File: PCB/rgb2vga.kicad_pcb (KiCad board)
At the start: 2 copper layers, 70.5 x 55.9 mm, 39 parts, among them J1 GPIO_0, J2 RGB_IN, J3 COCO3_RGB_IN, J4 C_VIDEO_IN, J5 GPIO_1, J6 VGA_OUT, SW1 SW_DIP_x12, U1 LM1881

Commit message: SW2 for Artifact
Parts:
- added SW2: SW_DP3T, 000_LOCAL:SW_DP3T_CK_JS203011JAQN, B.Cu at (143.2, 126.7)
- SW1: value SW_DIP_x12 -> SW_DIP_x10; footprint 000_LOCAL:SW_DIP_SPSTx12_Slide_6.7x32.04mm_W8.61mm_P2.54mm_LowProfile -> 000_LOCAL:SW_DIP_SPSTx10_Slide_6.7_8.61_P2.54_LowProfile
- moved R24 3.19 mm to (143.2, 117.5)
- moved SW1 1.27 mm to (130.8, 101.0)
- moved R1 0.32 mm to (155.3, 101.0)
- moved R10 0.32 mm to (155.3, 78.1)
- moved R11 0.32 mm to (155.3, 126.4)
- moved R12 0.32 mm to (155.3, 121.3)
- moved R13 0.32 mm to (155.3, 111.1)
- moved R14 0.32 mm to (155.3, 116.2)
- moved R15 0.32 mm to (155.3, 118.7)
- moved R16 0.32 mm to (155.3, 123.8)
- moved R17 0.32 mm to (155.3, 113.7)
- moved R2 0.32 mm to (155.3, 98.4)
- moved R26 0.32 mm to (155.3, 80.6)
- moved R3 0.32 mm to (155.3, 95.9)
- moved R4 0.32 mm to (155.3, 93.3)
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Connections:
- J3 pad 10: (no net) -> GND
- SW1 pad 1: (no net) -> /RGB_G
- SW1 pad 10: /SW_SCANLINE -> /_VSYNC
- SW1 pad 11: /_HSYNC -> /SW_C_VS
- SW1 pad 12: /_VSYNC -> /SW_C_HS
- SW1 pad 13: /SW_C_VS -> GND
- SW1 pad 14: /SW_C_HS -> GND
- SW1 pad 2: /RGB_G -> /SW_SHRINK
- SW1 pad 20: GND -> /RGB_CS
- SW1 pad 3: /SW_SHRINK -> /SW_MSX
- SW1 pad 4: /SW_MSX -> /SW_DEINT
- SW1 pad 5: /SW_DEINT -> /SW_APPLE_][
- SW1 pad 6: /SW_APPLE_][ -> GND
- SW1 pad 7: /SW_ARTIF_INV -> /SW_SYNC_LVL
- SW1 pad 8: /SW_ARTIFACT -> /SW_SCANLINE
- SW1 pad 9: /SW_SYNC_LVL -> /_HSYNC
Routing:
- net /SW_ARTIF_INV: track 3.71 -> 59.1 mm, vias 0 -> 1
- net /SW_ARTIFACT: track 3.71 -> 55.2 mm, vias 0 -> 1
- net /DIFF_N: track 85.2 -> 88.5 mm
- net /D0: track 30.8 -> 32.9 mm
- net /D2: track 30.8 -> 31.7 mm
- net /RGB_V: track 38.9 -> 38.0 mm
- net /RGB_CS: track 74.4 -> 73.5 mm
- net /VGA_B: track 44.0 -> 43.4 mm
- net /D1: track 30.9 -> 30.4 mm
- net /SW_C_VS: track 16.9 -> 16.4 mm
- net /_HSYNC: track 37.9 -> 38.4 mm
- net /_VSYNC: track 28.7 -> 29.2 mm
- net /SW_C_HS: track 16.9 -> 16.4 mm
- net /SW_SHRINK: track 3.71 -> 3.19 mm
- net /SW_MSX: track 3.71 -> 3.19 mm
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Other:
- board text added: "DE0-Nano"
- board text added: "INV"
- board text added: "OFF"
- board text added: "ON"
- board text added: "USB"
- board text added: "github.com/bkw777/rgb2vga - v005"
- board text removed: "ART. INV."
- board text removed: "github.com/bkw777/rgb2vga - v004.5"

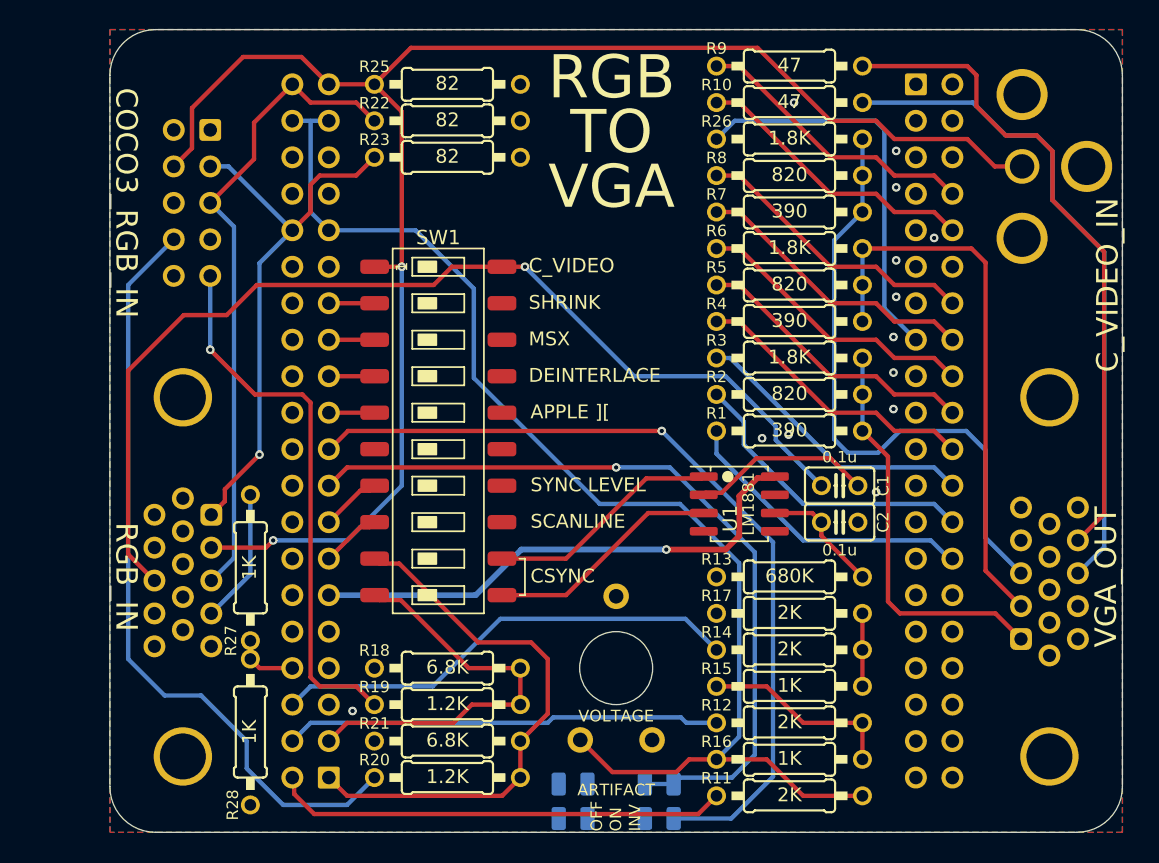
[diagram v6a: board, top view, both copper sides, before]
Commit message: align & center parts, silkscreen
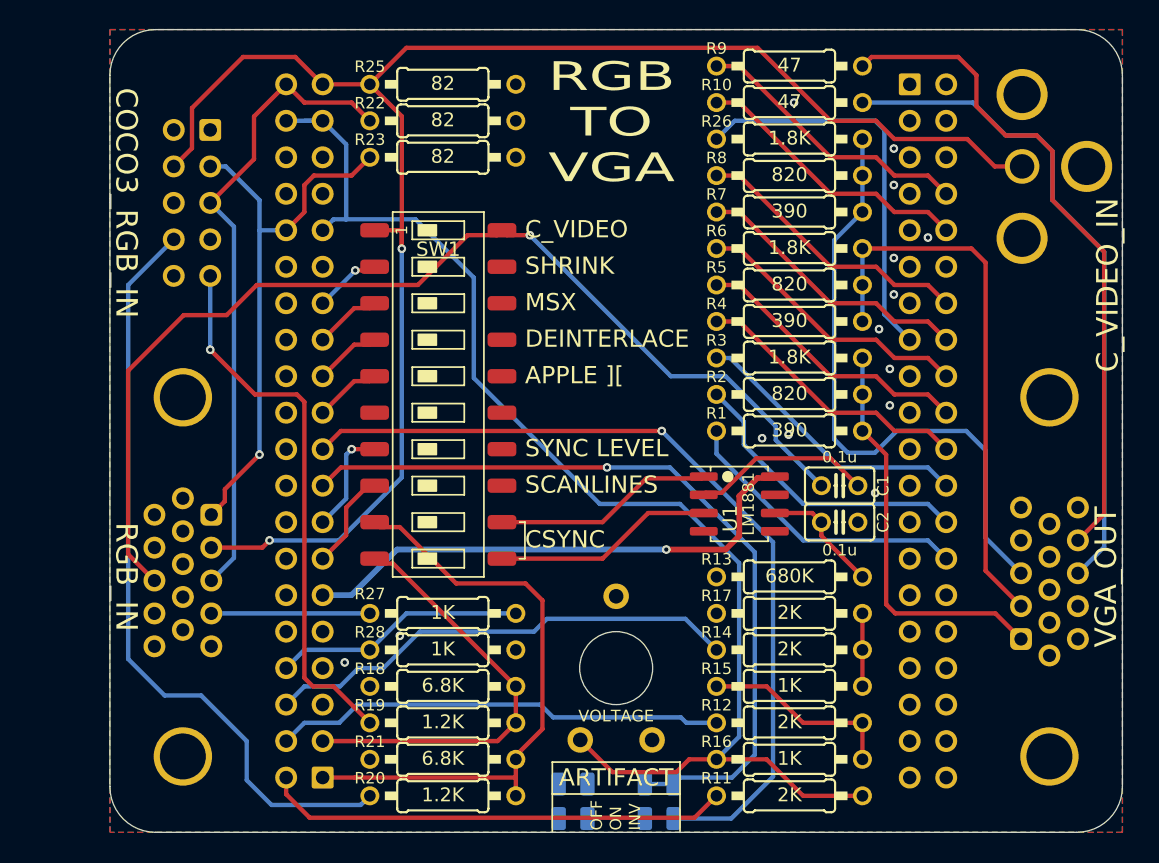
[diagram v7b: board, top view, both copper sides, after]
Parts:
- moved R28 14.6 mm to (131.1, 116.2), turned to 0 degrees
- moved R27 13.8 mm to (131.1, 113.7), turned to 0 degrees
- moved SW1 2.54 mm to (130.8, 98.4)
- moved R18 1.31 mm to (131.1, 118.7)
- moved R19 1.31 mm to (131.1, 121.3)
- moved R20 1.31 mm to (131.1, 126.4)
- moved R21 1.31 mm to (131.1, 123.8)
- moved REF** 0.44 mm to (143.2, 103.7)
- moved J5 0.43 mm to (163.6, 76.8)
- moved J1 0.43 mm to (122.8, 125.1)
- moved R22 0.32 mm to (131.1, 79.4)
- moved R23 0.32 mm to (131.1, 81.9)
- moved R25 0.32 mm to (131.1, 76.8)
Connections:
- R27 pad 1: /_BRIGHT -> /RGB_BR
- R27 pad 2: /RGB_BR -> /_BRIGHT
- R28 pad 1: GND -> /_BRIGHT
- R28 pad 2: /_BRIGHT -> GND
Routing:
- net /_BRIGHT: track 4.45 -> 17.6 mm
- net /_HSYNC: track 38.4 -> 41.8 mm
- net /SW_SYNC_LVL: track 4.24 -> 7.52 mm, vias 0 -> 1
- net /SW_SCANLINE: track 4.24 -> 6.85 mm
- net /DIFF_N: track 88.5 -> 90.7 mm
- net /RGB_CS: track 73.5 -> 75.6 mm
- net /RGB_BR: track 9.39 -> 11.0 mm
- net /SW_SHRINK: track 3.19 -> 4.68 mm, vias 0 -> 1
- net /SW_DEINT: track 3.19 -> 4.67 mm
- net /SW_MSX: track 3.19 -> 4.67 mm
- net /SW_APPLE_][: track 3.19 -> 4.67 mm
- net /D1: track 30.4 -> 31.5 mm
- net /RGB_G: track 114.8 -> 115.9 mm
- net /SW_C_HS: track 16.4 -> 15.4 mm
- net /SW_C_VS: track 16.4 -> 15.4 mm
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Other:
- board text added: "SCANLINES"
- board text added: "github.com/bkw777/rgb2vga - v006"
- board text removed: "SCANLINE"
- board text removed: "github.com/bkw777/rgb2vga - v005"

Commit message: isolisolate r,g,b in a little better, cosmetic alignment
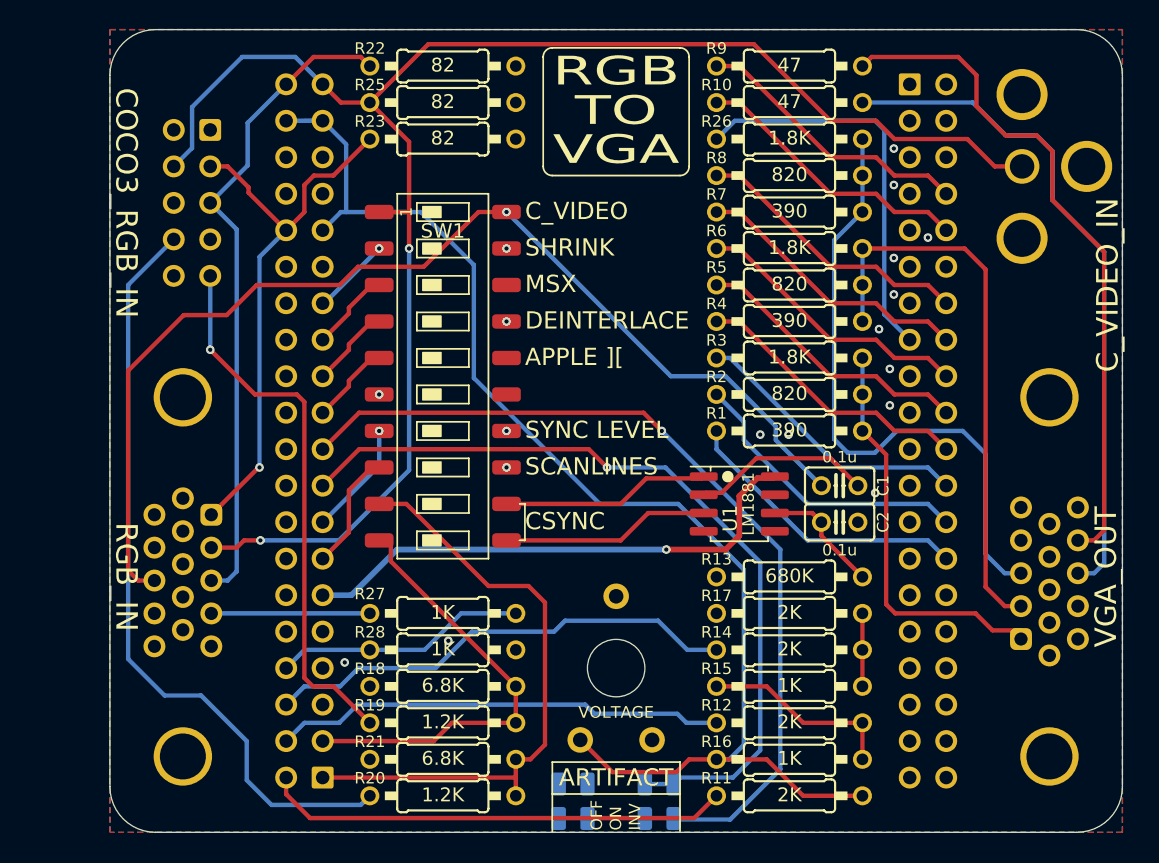
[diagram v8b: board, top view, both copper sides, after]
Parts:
- J1, J5: footprint 000_LOCAL:PinSocket_2x20_P2.54mm_Vertical -> 000_LOCAL:PinSocket_2x20_P2.54mm_Polarized_Vertical
- REF**: value DE0-Nano_no_cover -> DE0-Nano_bare; footprint 000_LOCAL:DE0-Nano_no_cover -> 000_LOCAL:DE0-Nano_bare
- moved R22 3.81 mm to (131.1, 75.6)
- moved SW1 1.31 mm to (131.1, 97.2)
- moved R23 1.27 mm to (131.1, 80.6)
- moved R25 1.27 mm to (131.1, 78.1)
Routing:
- net /RGB_CS: track 75.6 -> 77.3 mm
- net /SW_ARTIF_INV: track 59.5 -> 61.1 mm
- net /SW_SCANLINE: track 6.85 -> 8.29 mm
- net /SW_ARTIFACT: track 55.7 -> 56.9 mm
- net /DIFF_N: track 90.7 -> 91.8 mm
- net /SW_DEINT: track 4.67 -> 5.75 mm
- net /SW_MSX: track 4.67 -> 5.75 mm
- net /SW_APPLE_][: track 4.67 -> 5.75 mm
- net /_VSYNC: track 30.0 -> 31.1 mm
- net /_HSYNC: track 41.8 -> 42.7 mm
- net /SW_C_VS: track 15.4 -> 14.5 mm
- net /SW_C_HS: track 15.4 -> 14.5 mm
- net /SW_SHRINK: track 4.68 -> 5.51 mm
- net /RGB_B: track 44.9 -> 45.8 mm
- net /VGA_V: track 46.8 -> 47.5 mm
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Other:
- board text added: "github.com/bkw777/rgb2vga - v008"
- board text removed: "github.com/bkw777/rgb2vga - v006"
